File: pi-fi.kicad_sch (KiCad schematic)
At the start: 27 parts, among them J3 Conn_02x04, J5 EEPROM WP, J6 GPIO Header, U3 74LVC1G07

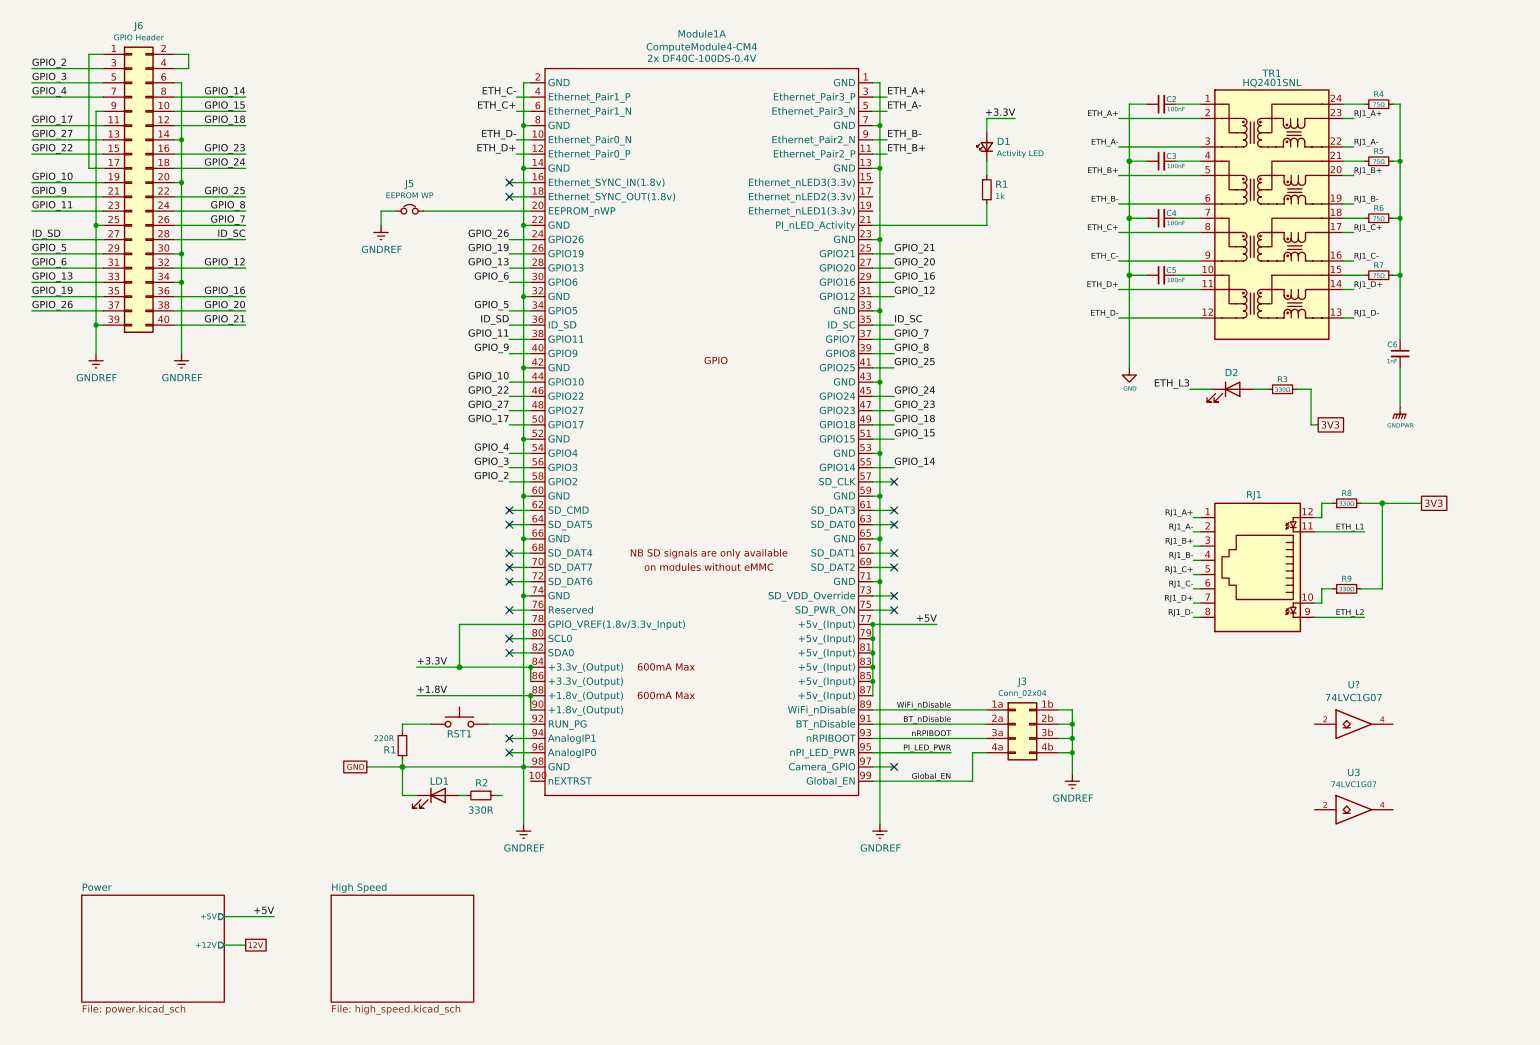
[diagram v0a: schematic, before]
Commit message: sd card, power LED, mounting holes
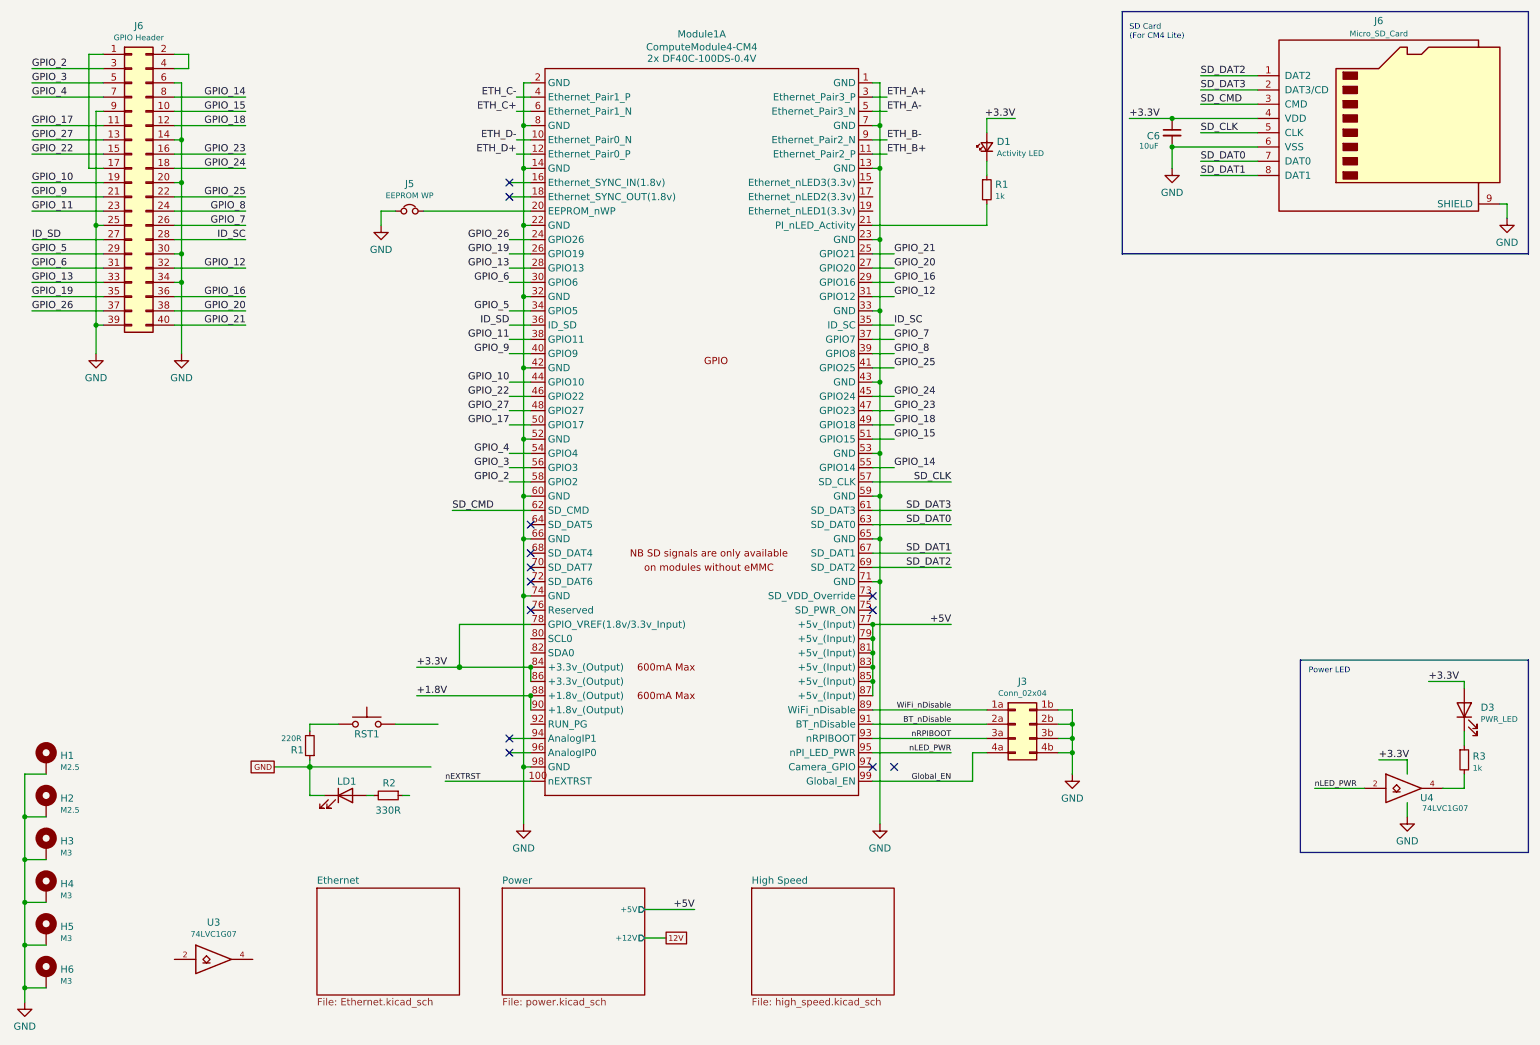
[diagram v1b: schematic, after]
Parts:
- removed C2, C3, C4, C5: 100nF, KiCad/kicad-footprints/Capacitor_SMD.pretty:C_0805_2012Metric_Pad1.15x1.40mm_HandSolder, symbol Device:C_Small
- removed D2: LED, KiCad/kicad-footprints/LED_SMD.pretty:LED_0805_2012Metric_Pad1.15x1.40mm_HandSolder, symbol Device:LED
- removed R4, R5, R6, R7: 75Ω, KiCad/Resistors_SMD.pretty:R_0805_HandSoldering, symbol Device:R_Small
- removed R8, R9: 330Ω, KiCad/Resistors_SMD.pretty:R_0805_HandSoldering, symbol Device:R_Small
- removed RJ1: RJ45, KiCad/kicad-footprints/Connector_RJ.pretty:RJ45_Amphenol_RJHSE538X, symbol Connector:RJ45_LED
- removed TR1: HQ2401SNL, Custom Footprints:HQ2401SNL, symbol CustomSymbols:HQ2401SNL
- added D3: PWR_LED, symbol Device:LED
- added H1, H2: M2.5, KiCad/kicad-footprints/MountingHole.pretty:MountingHole_2.7mm_M2.5_Pad, symbol Mechanical:MountingHole_Pad
- added H3, H4, H5, H6: M3, KiCad/kicad-footprints/MountingHole.pretty:MountingHole_3.2mm_M3_Pad_Via, symbol Mechanical:MountingHole_Pad
- added J6: Micro_SD_Card, KiCad/kicad-footprints/Connector_Card.pretty:microSD_HC_Molex_104031-0811, symbol Connector:Micro_SD_Card
- C6: value 1nF -> 10uF; footprint KiCad/Capacitors_SMD.pretty:C_0805_HandSoldering -> KiCad/kicad-footprints/Capacitor_SMD.pretty:C_0603_1608Metric
- R3: value 330Ω -> 1k; footprint KiCad/Resistors_SMD.pretty:R_0805_HandSoldering -> (none)
- gave numbers to parts that had none: 1
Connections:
- net +3.3V is gone; now on net VCC: D1.2 (A), Module1.78 (GPIO_VREF(1.8v/3.3v_Input)), Module1.84 (+3.3v_(Output)), Module1.86 (+3.3v_(Output))
- net 3V3 is gone; now on an unnamed net: R3.2
- net GNDPWR is gone; now on net GND: C6.2
- net PI_LED_PWR is gone; now on net nLED_PWR: Module1.95 (nPI_LED_PWR)
- net GND: now also H1.1, H2.1, H3.1, H4.1, H5.1, H6.1, J6.6 (VSS), J6.9 (SHIELD)
- net VCC: now also C6.1, D3.2 (A), J6.4 (VDD)
- net at R3.1: now also D3.1 (K)
- net nEXTRST: now reaches Module1.100 (nEXTRST)
- net SD_CLK: now reaches Module1.57 (SD_CLK)
- net SD_CLK: now also J6.5 (CLK)
- net SD_DAT3: now reaches Module1.61 (SD_DAT3)
- net SD_DAT3: now also J6.2 (DAT3/CD)
- net SD_CMD: now reaches Module1.62 (SD_CMD)
- net SD_CMD: now also J6.3 (CMD)
- net SD_DAT0: now reaches Module1.63 (SD_DAT0)
- net SD_DAT0: now also J6.7 (DAT0)
- net SD_DAT1: now reaches Module1.67 (SD_DAT1)
- net SD_DAT1: now also J6.8 (DAT1)
- net SD_DAT2: now reaches Module1.69 (SD_DAT2)
- net SD_DAT2: now also J6.1 (DAT2)
- net at RST1.3 (B), RST1.4 (B): no longer Module1.92 (RUN_PG)
- net nLED_PWR: now reaches U4.2
- no-connect marks 20 -> 13
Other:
- added sheet Ethernet (Ethernet.kicad_sch)
- note added: "Power LED"
- note added: "SD Card (For CM4 Lite)"
- moved on the sheet: LD1, R1, R2, RST1, U3, U4
